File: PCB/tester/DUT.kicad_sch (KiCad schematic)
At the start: 72 parts, among them J3 6pin_hd, J4 Conn_02x03_Odd_Even, J5 MotorCkeck1, J6 MotorCkeck2, J7 Conn_01x02_Socket, K1 Relay SPDT, K2 Relay SPDT, K3 Relay SPDT, Q2 PMF170XP,115, Q3 DMN63D8L-7, Q4 DMN63D8L-7, Q5 DMN63D8L-7, Q6 DMN63D8L-7, U6 THS4281, U7 THS4281, U8 THS4281, U9 ZXCT1082

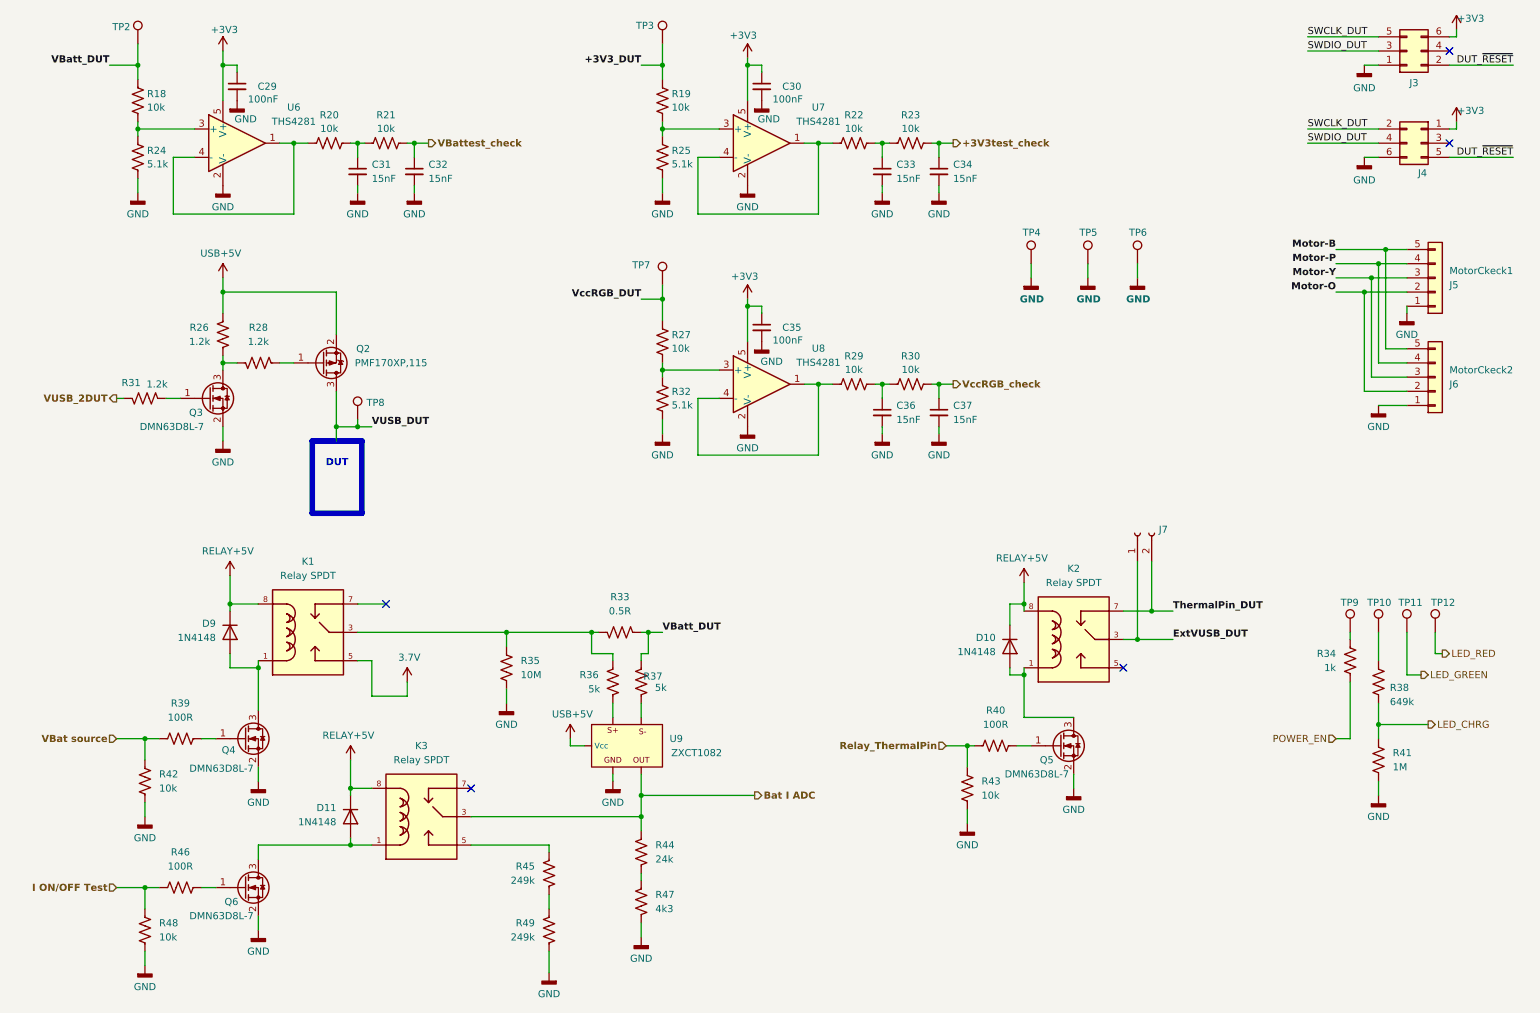
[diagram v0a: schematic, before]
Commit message: promenores componentes para a BOM
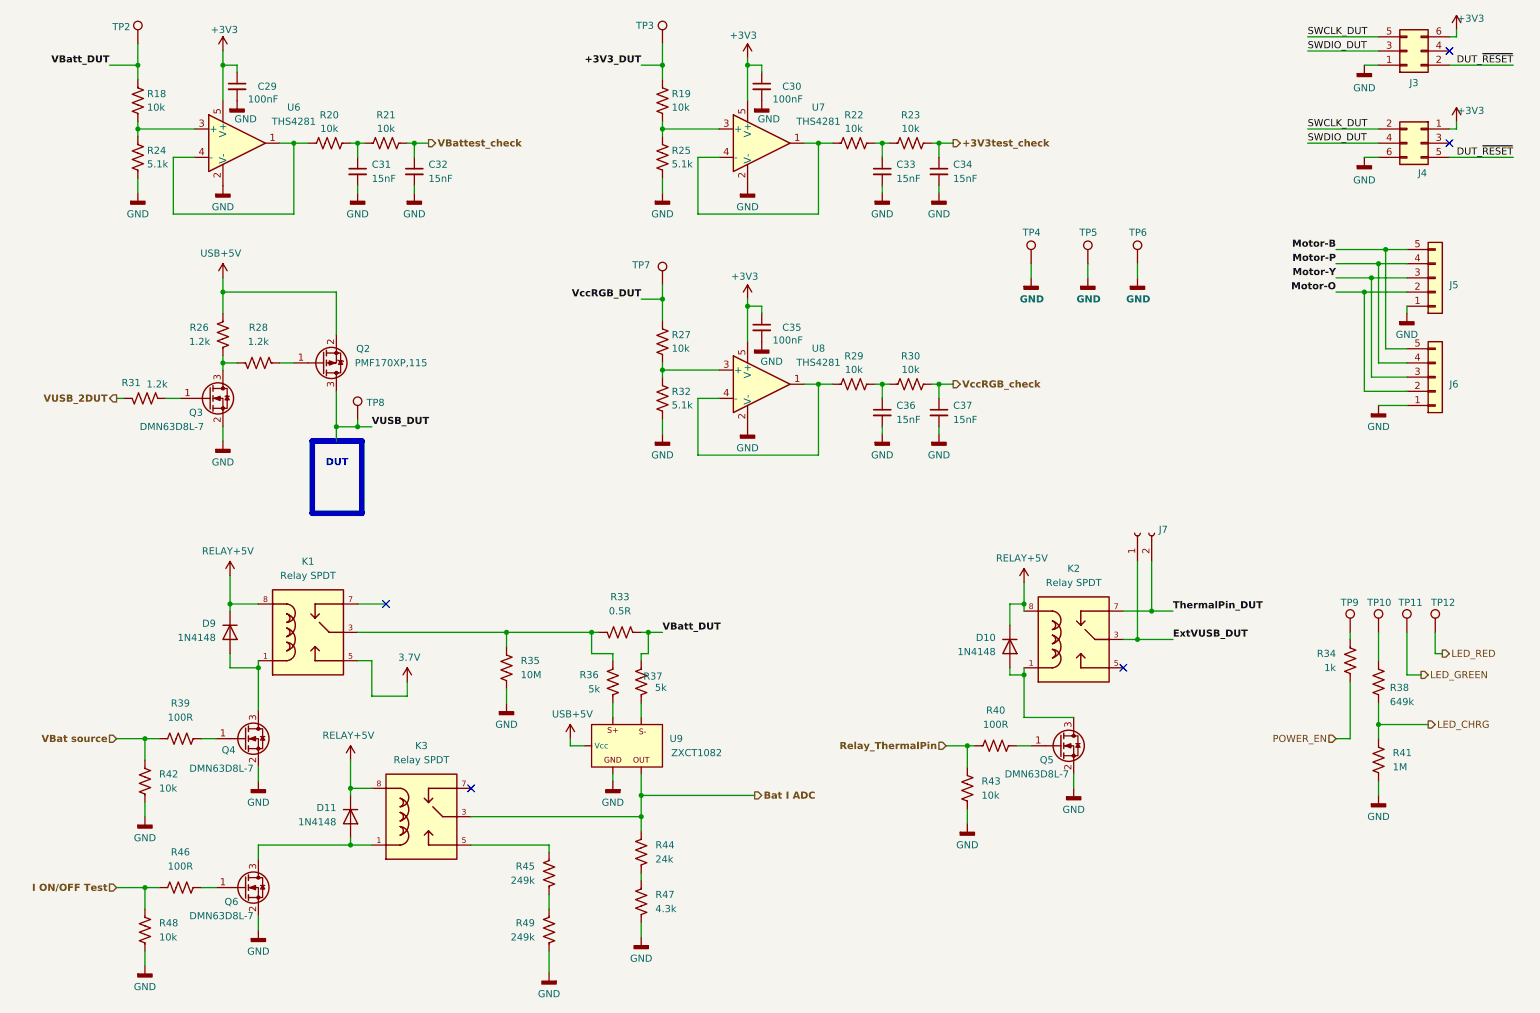
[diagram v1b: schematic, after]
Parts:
- J4: value Conn_02x03_Odd_Even -> 61300621021
- J5: value MotorCkeck1 -> PPTC051LFBN-RC
- J6: value MotorCkeck2 -> 61300511021
- J7: value Conn_01x02_Socket -> PPTC021LFBN-RC
- R45, R49: Tolerance 0.1% -> 1%
- R47: value 4k3 -> 4.3k; Tolerance 1% -> 5%
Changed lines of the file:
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@@
 			)
 		)
-		(property "Value" "MotorCkeck1"
+		(property "Value" "PPTC051LFBN-RC"
 			(at 267.97 64.7701 0)
+			(hide yes)
 			(show_name no)
 			(do_not_autoplace no)
@@
 			)
 		)
-		(property "Value" "MotorCkeck2"
+		(property "Value" "61300511021"
 			(at 267.97 82.5501 0)
+			(hide yes)
 			(show_name no)
 			(do_not_autoplace no)
@@
 			)
 		)
-		(property "Tolerance" "0.1%"
+		(property "Tolerance" "1%"
 			(at 106.68 182.88 0)
 			(hide yes)
@@
 			)
 		)
-		(property "Tolerance" "0.1%"
+		(property "Tolerance" "1%"
 			(at 106.68 172.72 0)
 			(hide yes)
@@
 			)
 		)
-		(property "Value" "Conn_02x03_Odd_Even"
+		(property "Value" "61300621021"
 			(at 261.62 46.99 0)
 			(hide yes)
@@
 			)
 		)
-		(property "Value" "Conn_01x02_Socket"
+		(property "Value" "PPTC021LFBN-RC"
 			(at 215.9 113.6649 90)
 			(hide yes)
@@
 			)
 		)
-		(property "Value" "4k3"
+		(property "Value" "4.3k"
 			(at 125.73 179.0699 0)
 			(show_name no)
@@
 			)
 		)
-		(property "Tolerance" "1%"
+		(property "Tolerance" "5%"
 			(at 123.19 177.8 0)
 			(hide yes)
